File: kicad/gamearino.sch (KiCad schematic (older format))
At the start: 11 parts, among them Q3 PMBT3904, Q4 PMBT3906, SW1 Left, SW2 Up, SW3 Down, SW4 Right, SW5 Select, SW6 Start, SW7 B, SW8 A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

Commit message: PCB-Platzierung, 3D-Knöpfe, Schaltung wird noch getestet
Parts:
- removed Q3: PMBT3904, Package_TO_SOT_SMD:SOT-23, symbol Device:Q_NPN_BEC
- removed Q4: PMBT3906, Package_TO_SOT_SMD:SOT-23, symbol Device:Q_PNP_BEC
- removed SW1: Left, htl_smd:SW_Push_5.1mm_H1.5mm, symbol Switch:SW_Push
- removed SW2: Up, htl_smd:SW_Push_5.1mm_H1.5mm, symbol Switch:SW_Push
- removed SW3: Down, htl_smd:SW_Push_5.1mm_H1.5mm, symbol Switch:SW_Push
- removed SW4: Right, htl_smd:SW_Push_5.1mm_H1.5mm, symbol Switch:SW_Push
- removed SW5: Select, htl_smd:SW_Push_5.1mm_H1.5mm, symbol Switch:SW_Push
- removed SW6: Start, htl_smd:SW_Push_5.1mm_H1.5mm, symbol Switch:SW_Push
- removed SW7: B, htl_smd:SW_Push_5.1mm_H1.5mm, symbol Switch:SW_Push
- removed SW8: A, htl_smd:SW_Push_5.1mm_H1.5mm, symbol Switch:SW_Push
- added H1, H2, H3, H4: MountingHole, MountingHole:MountingHole_3.2mm_M3, symbol Mechanical:MountingHole
- added Item1: 3D Druck: Knopf A, gamearino:ABKnopf, symbol htl_virtual:Item
- added Item2: 3D Druck: Knopf B, gamearino:ABKnopf, symbol htl_virtual:Item
- added Item3: 3D Druck: Knopf Start, gamearino:StartSelect, symbol htl_virtual:Item
- added Item4: 3D Druck: Knopf Select, gamearino:StartSelect, symbol htl_virtual:Item
- added Item5: 3D Druck: Steuerkreuz, gamearino:Steuerkreuz_zeik, symbol htl_virtual:Item
- added Item6: PCB: Abmessungen?, 2 Layer, 35u Cu, d1,6mm, symbol htl_virtual:Item
- added Item7: SMD-Schablone: 120um, Edelstahl, 25mm Umlaufender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, symbol htl_virtual:Item
- added R1, R2: 10k, Resistor_SMD:R_0603_1608Metric, symbol Device:R
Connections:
- net labels added: +3.3V, +3V3, GNDD
- wire segments 0 -> 45
- no-connect marks 0 -> 1
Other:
- note added: "Arduino-IDE:\nProgrammierbar über die Standardeinstellungen\nfür NodeMCU V1.0"
- note added: "Enable Pin:\nmuss über 10k auf 3V3 liegen"
- note added: "GPIO0 - Bootmode: \nlow=bootloader, \nhigh=flashboot"
- note added: "GPIO15:\nmuss beim Booten über 10k\nauf GND liegen. Dann kann er\nverwendet werden."
- note added: "TODO: SDA/SCL an ESP ausprobieren"
- moved on the sheet: U1

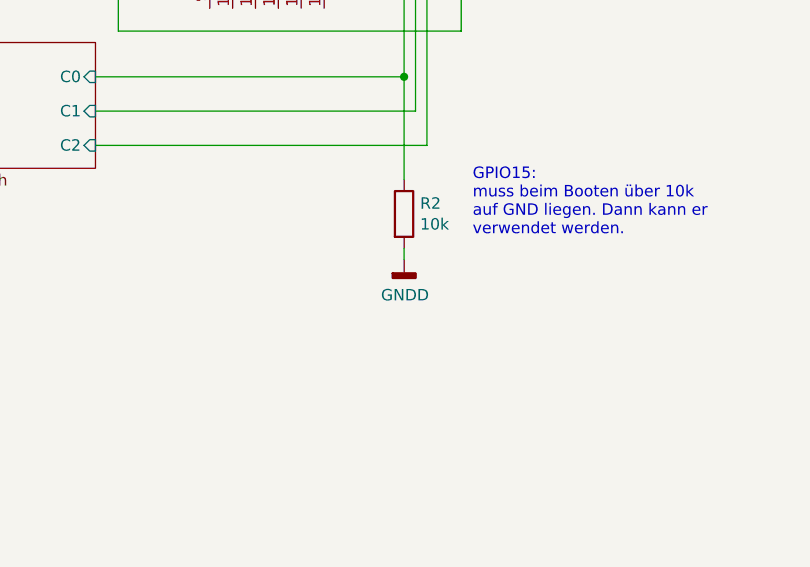
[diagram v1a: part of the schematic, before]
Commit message: Changelog eingeführt, GND statt GNDD
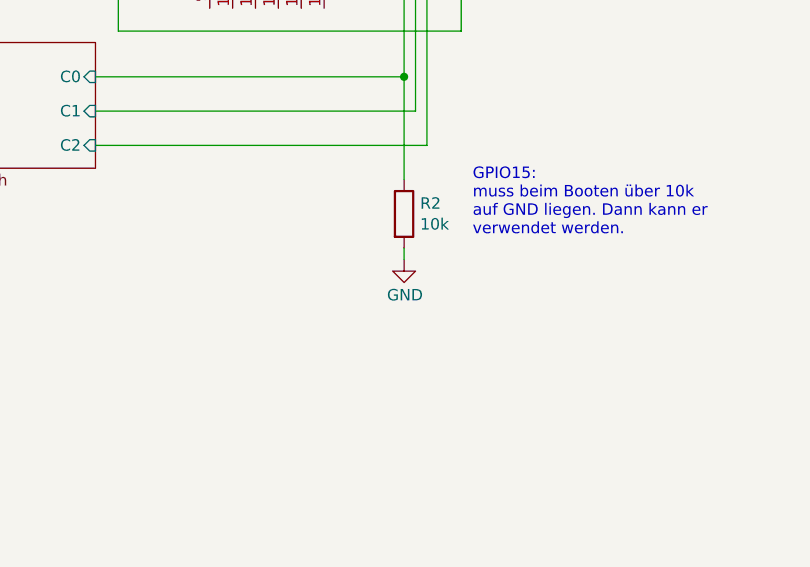
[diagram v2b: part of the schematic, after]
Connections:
- net GNDD renamed GND
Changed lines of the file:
@@
 	6350 3950 6300 3950
 $Comp
-L power:GNDD #PWR?
+L power:GND #PWR?
 U 1 1 6040EFD2
 P 6350 5550
@@
 AR Path="/6040EFD2" Ref="#PWR02"  Part="1"
 F 0 "#PWR02" H 6350 5300 50  0001 C CNN
-F 1 "GNDD" H 6354 5395 50  0000 C CNN
+F 1 "GND" H 6354 5395 50  0000 C CNN
 F 2 "" H 6350 5550 50  0001 C CNN
 F 3 "" H 6350 5550 50  0001 C CNN

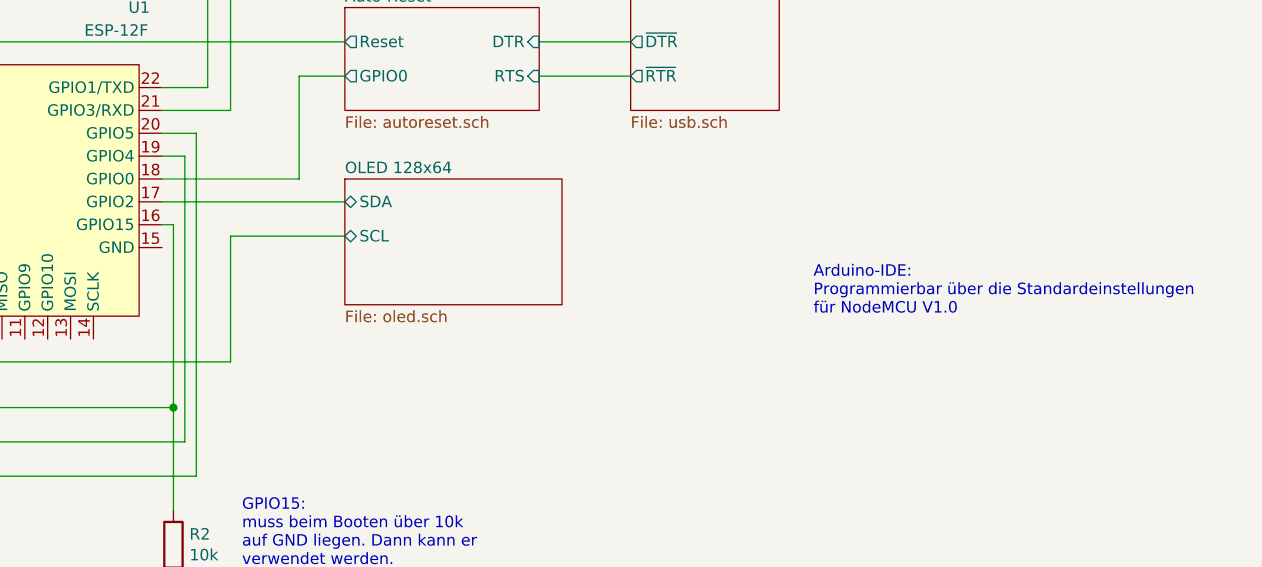
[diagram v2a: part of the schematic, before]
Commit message: usb.sch Datei war gebrochen, wurde gefixt
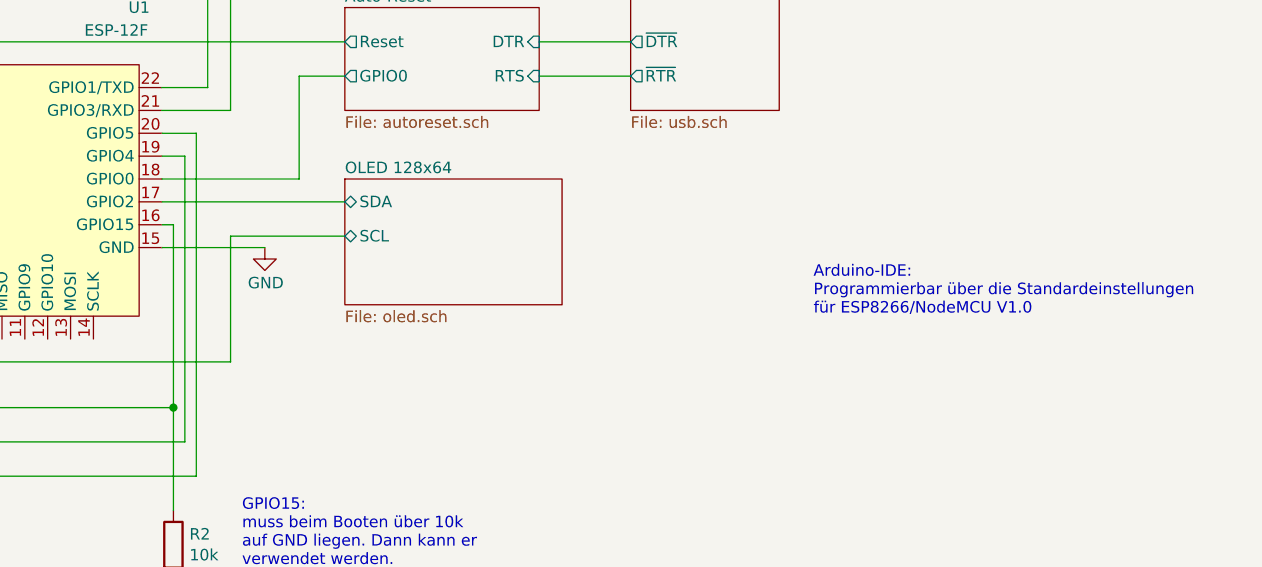
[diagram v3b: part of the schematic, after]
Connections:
- net GND: now also U1.15 (GND)
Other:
- note added: "Arduino-IDE:\nProgrammierbar über die Standardeinstellungen\nfür ESP8266/NodeMCU V1.0"
- note removed: "Arduino-IDE:\nProgrammierbar über die Standardeinstellungen\nfür NodeMCU V1.0"
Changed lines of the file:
@@
 GPIO15:\nmuss beim Booten über 10k\nauf GND liegen. Dann kann er\nverwendet werden.
 Text Notes 9150 4350 0    50   ~ 0
-Arduino-IDE:\nProgrammierbar über die Standardeinstellungen\nfür NodeMCU V1.0
+Arduino-IDE:\nProgrammierbar über die Standardeinstellungen\nfür ESP8266/NodeMCU V1.0
 $Comp
 L htl_virtual:Item Item1
@@
 	1    0    0    -1
 $EndComp
+$Comp
+L power:GND #PWR?
+U 1 1 60538B2A
+P 6750 4050
+AR Path="/5F8674B3/60538B2A" Ref="#PWR?"  Part="1"
+AR Path="/60538B2A" Ref="#PWR?"  Part="1"
+F 0 "#PWR?" H 6750 3800 50  0001 C CNN
+F 1 "GND" H 6754 3895 50  0000 C CNN
+F 2 "" H 6750 4050 50  0001 C CNN
+F 3 "" H 6750 4050 50  0001 C CNN
+	1    6750 4050
+	1    0    0    -1
+$EndComp
+Wire Wire Line
+	6300 4050 6750 4050
 $EndSCHEMATC

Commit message: Pinliste und kleinere Verschönerungen, Transistor-Value, ...
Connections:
- no-connect marks 1 -> 7
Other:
- note added: "TODO: SDA-Leitung macht \ndas Flashen aktuell unmöglich."
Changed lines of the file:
@@
 Wire Wire Line
 	6300 4050 6750 4050
+NoConn ~ 5500 4450
+NoConn ~ 5600 4450
+NoConn ~ 5700 4450
+NoConn ~ 5800 4450
+NoConn ~ 5900 4450
+NoConn ~ 6000 4450
+Text Notes 7150 4700 0    50   ~ 0
+TODO: SDA-Leitung macht \ndas Flashen aktuell unmöglich.
+Wire Notes Line
+	7100 4600 6800 3850
 $EndSCHEMATC

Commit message: OLED funktioniert, Gehäuse vorläufig fertig
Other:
- note added: "TODO: Neue 3D-Modelle verwenden"
- note added: "TODO: Taster ausprobieren"
- note removed: "TODO: SDA-Leitung macht \ndas Flashen aktuell unmöglich."
- note removed: "TODO: SDA/SCL an ESP ausprobieren"
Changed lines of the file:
@@
 Text Notes 5950 2300 0    50   ~ 0
 GPIO0 - Bootmode: \nlow=bootloader, \nhigh=flashboot
-Text Notes 1050 750  0    50   ~ 0
-TODO: SDA/SCL an ESP ausprobieren
 Wire Wire Line
 	6300 3350 6500 3350
@@
 NoConn ~ 5900 4450
 NoConn ~ 6000 4450
-Text Notes 7150 4700 0    50   ~ 0
-TODO: SDA-Leitung macht \ndas Flashen aktuell unmöglich.
-Wire Notes Line
-	7100 4600 6800 3850
+Text Notes 3750 5700 0    50   ~ 0
+TODO: Taster ausprobieren
+Text Notes 2050 6350 0    50   ~ 0
+TODO: Neue 3D-Modelle verwenden
 $EndSCHEMATC

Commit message: v0.0.1 für CNC-Fertigung
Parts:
- H1, H2, H3, H4: footprint MountingHole:MountingHole_3.2mm_M3 -> htl_mechanical:MountingHole_3.2mm_M3
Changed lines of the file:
@@
 F 0 "H1" H 10400 5796 50  0000 L CNN
 F 1 "MountingHole" H 10400 5705 50  0000 L CNN
-F 2 "MountingHole:MountingHole_3.2mm_M3" H 10300 5750 50  0001 C CNN
+F 2 "htl_mechanical:MountingHole_3.2mm_M3" H 10300 5750 50  0001 C CNN
 F 3 "~" H 10300 5750 50  0001 C CNN
 	1    10300 5750
@@
 F 0 "H2" H 10400 5996 50  0000 L CNN
 F 1 "MountingHole" H 10400 5905 50  0000 L CNN
-F 2 "MountingHole:MountingHole_3.2mm_M3" H 10300 5950 50  0001 C CNN
+F 2 "htl_mechanical:MountingHole_3.2mm_M3" H 10300 5950 50  0001 C CNN
 F 3 "~" H 10300 5950 50  0001 C CNN
 	1    10300 5950
@@
 F 0 "H3" H 10400 6196 50  0000 L CNN
 F 1 "MountingHole" H 10400 6105 50  0000 L CNN
-F 2 "MountingHole:MountingHole_3.2mm_M3" H 10300 6150 50  0001 C CNN
+F 2 "htl_mechanical:MountingHole_3.2mm_M3" H 10300 6150 50  0001 C CNN
 F 3 "~" H 10300 6150 50  0001 C CNN
 	1    10300 6150
@@
 F 0 "H4" H 10400 6396 50  0000 L CNN
 F 1 "MountingHole" H 10400 6305 50  0000 L CNN
-F 2 "MountingHole:MountingHole_3.2mm_M3" H 10300 6350 50  0001 C CNN
+F 2 "htl_mechanical:MountingHole_3.2mm_M3" H 10300 6350 50  0001 C CNN
 F 3 "~" H 10300 6350 50  0001 C CNN
 	1    10300 6350
@@
 P 6750 4050
 AR Path="/5F8674B3/60538B2A" Ref="#PWR?"  Part="1"
-AR Path="/60538B2A" Ref="#PWR?"  Part="1"
-F 0 "#PWR?" H 6750 3800 50  0001 C CNN
+AR Path="/60538B2A" Ref="#PWR0102"  Part="1"
+F 0 "#PWR0102" H 6750 3800 50  0001 C CNN
 F 1 "GND" H 6754 3895 50  0000 C CNN
 F 2 "" H 6750 4050 50  0001 C CNN

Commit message: Fertiges Layout v0.0.2, 3 Stk bestellt
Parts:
- added FID1, FID2: Fiducial, htl_mechanical:paste-fiducial, symbol Mechanical:Fiducial
- Item1, Item2: footprint gamearino:ABKnopf -> gamearino:ABKnopf_v2
- Item3, Item4: footprint gamearino:StartSelect -> gamearino:StartSelect_v2
- Item5: footprint gamearino:Steuerkreuz_zeik -> gamearino:Steuerkreuz_zeik_v2
- U1: DistOrderNr (none) -> C82891; Distributor (none) -> LCSC; ManPartNr (none) -> ESP-12F(ESP8266MOD); Manufacturer (none) -> Ai-Thinker; PriceEUR (none) -> 1.24; PriceForQty (none) -> 100; Weblink (none) -> https://lcsc.com/product-detail/WiFi-Modules_Ai-Thinker-ESP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
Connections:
- net EN: now reaches R1.2, U1.3 (EN)
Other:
- note removed: "TODO: Neue 3D-Modelle verwenden"
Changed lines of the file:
@@
 Sheet 1 5
 Title "Gamearino"
-Date "2020-10-13"
-Rev "20.0.0-dev"
+Date "2021-04-29"
+Rev "V0.0.2"
 Comp "HTL-Steyr"
 Comment1 "4ABHEL, 2020/2021"
-Comment2 ""
+Comment2 "Hosted by Prof. Karl Zeilhofer"
 Comment3 ""
 Comment4 ""
@@
 F 2 "htl_modules:ESP-12F" H 5750 3850 50  0001 C CNN
 F 3 "http://wiki.ai-thinker.com/_media/esp8266/esp8266_series_modules_user_manual_v1.1.pdf" H 5400 3950 50  0001 C CNN
+F 4 "C82891" H 5750 3850 50  0001 C CNN "DistOrderNr"
+F 5 "LCSC" H 5750 3850 50  0001 C CNN "Distributor"
+F 6 "ESP-12F(ESP8266MOD)" H 5750 3850 50  0001 C CNN "ManPartNr"
+F 7 "Ai-Thinker" H 5750 3850 50  0001 C CNN "Manufacturer"
+F 8 "1.24" H 5750 3850 50  0001 C CNN "PriceEUR"
+F 9 "100" H 5750 3850 50  0001 C CNN "PriceForQty"
+F 10 "https://lcsc.com/product-detail/WiFi-Modules_Ai-Thinker-ESP-12F-ESP8266MOD_C82891.html" H 5750 3850 50  0001 C CNN "Weblink"
 	1    5750 3850
 	1    0    0    -1
@@
 P 4900 2850
 AR Path="/5F8674B3/60406C3E" Ref="#PWR?"  Part="1"
-AR Path="/60406C3E" Ref="#PWR01"  Part="1"
+AR Path="/60406C3E" Ref="#PWR02"  Part="1"
 AR Path="/603FCB6F/60406C3E" Ref="#PWR?"  Part="1"
-F 0 "#PWR01" H 4900 2700 50  0001 C CNN
+F 0 "#PWR02" H 4900 2700 50  0001 C CNN
 F 1 "+3.3V" H 4915 3023 50  0000 C CNN
 F 2 "" H 4900 2850 50  0001 C CNN
@@
 P 6350 5550
 AR Path="/5F8674B3/6040EFD2" Ref="#PWR?"  Part="1"
-AR Path="/6040EFD2" Ref="#PWR02"  Part="1"
-F 0 "#PWR02" H 6350 5300 50  0001 C CNN
+AR Path="/6040EFD2" Ref="#PWR03"  Part="1"
+F 0 "#PWR03" H 6350 5300 50  0001 C CNN
 F 1 "GND" H 6354 5395 50  0000 C CNN
 F 2 "" H 6350 5550 50  0001 C CNN
@@
 AR Path="/5FA85ABF/5F7FB5B8/60461F5A" Ref="#PWR?"  Part="1"
 AR Path="/5F8D661A/60461F5A" Ref="#PWR?"  Part="1"
-AR Path="/60461F5A" Ref="#PWR0101"  Part="1"
-F 0 "#PWR0101" H 4800 4100 50  0001 C CNN
+AR Path="/60461F5A" Ref="#PWR01"  Part="1"
+F 0 "#PWR01" H 4800 4100 50  0001 C CNN
 F 1 "+3V3" H 4815 4423 50  0000 C CNN
 F 2 "" H 4800 4250 50  0001 C CNN
@@
 F 0 "Item1" H 930 6346 50  0000 L CNN
 F 1 "3D Druck: Knopf A" H 930 6255 50  0000 L CNN
-F 2 "gamearino:ABKnopf" H 800 6230 50  0001 C CNN
+F 2 "gamearino:ABKnopf_v2" H 800 6230 50  0001 C CNN
 F 3 "~" V 800 6300 50  0001 C CNN
 	1    800  6300
@@
 F 0 "Item2" H 930 6546 50  0000 L CNN
 F 1 "3D Druck: Knopf B" H 930 6455 50  0000 L CNN
-F 2 "gamearino:ABKnopf" H 800 6430 50  0001 C CNN
+F 2 "gamearino:ABKnopf_v2" H 800 6430 50  0001 C CNN
 F 3 "~" V 800 6500 50  0001 C CNN
 	1    800  6500
@@
 F 0 "Item3" H 930 6746 50  0000 L CNN
 F 1 "3D Druck: Knopf Start" H 930 6655 50  0000 L CNN
-F 2 "gamearino:StartSelect" H 800 6630 50  0001 C CNN
+F 2 "gamearino:StartSelect_v2" H 800 6630 50  0001 C CNN
 F 3 "~" V 800 6700 50  0001 C CNN
 	1    800  6700
@@
 F 0 "Item4" H 930 6946 50  0000 L CNN
 F 1 "3D Druck: Knopf Select" H 930 6855 50  0000 L CNN
-F 2 "gamearino:StartSelect" H 800 6830 50  0001 C CNN
+F 2 "gamearino:StartSelect_v2" H 800 6830 50  0001 C CNN
 F 3 "~" V 800 6900 50  0001 C CNN
 	1    800  6900
@@
 F 0 "Item5" H 930 7146 50  0000 L CNN
 F 1 "3D Druck: Steuerkreuz" H 930 7055 50  0000 L CNN
-F 2 "gamearino:Steuerkreuz_zeik" H 800 7030 50  0001 C CNN
+F 2 "gamearino:Steuerkreuz_zeik_v2" H 800 7030 50  0001 C CNN
 F 3 "~" V 800 7100 50  0001 C CNN
 	1    800  7100
@@
 P 6750 4050
 AR Path="/5F8674B3/60538B2A" Ref="#PWR?"  Part="1"
-AR Path="/60538B2A" Ref="#PWR0102"  Part="1"
-F 0 "#PWR0102" H 6750 3800 50  0001 C CNN
+AR Path="/60538B2A" Ref="#PWR04"  Part="1"
+F 0 "#PWR04" H 6750 3800 50  0001 C CNN
 F 1 "GND" H 6754 3895 50  0000 C CNN
 F 2 "" H 6750 4050 50  0001 C CNN
@@
 Text Notes 3750 5700 0    50   ~ 0
 TODO: Taster ausprobieren
-Text Notes 2050 6350 0    50   ~ 0
-TODO: Neue 3D-Modelle verwenden
+Text Label 5000 3550 0    30   ~ 0
+EN
+$Comp
+L Mechanical:Fiducial FID1
+U 1 1 6090F4D5
+P 9500 5800
+F 0 "FID1" H 9585 5846 50  0000 L CNN
+F 1 "Fiducial" H 9585 5755 50  0000 L CNN
+F 2 "htl_mechanical:paste-fiducial" H 9500 5800 50  0001 C CNN
+F 3 "~" H 9500 5800 50  0001 C CNN
+	1    9500 5800
+	1    0    0    -1
+$EndComp
+$Comp
+L Mechanical:Fiducial FID2
+U 1 1 6090F84F
+P 9500 6000
+F 0 "FID2" H 9585 6046 50  0000 L CNN
+F 1 "Fiducial" H 9585 5955 50  0000 L CNN
+F 2 "htl_mechanical:paste-fiducial" H 9500 6000 50  0001 C CNN
+F 3 "~" H 9500 6000 50  0001 C CNN
+	1    9500 6000
+	1    0    0    -1
+$EndComp
 $EndSCHEMATC

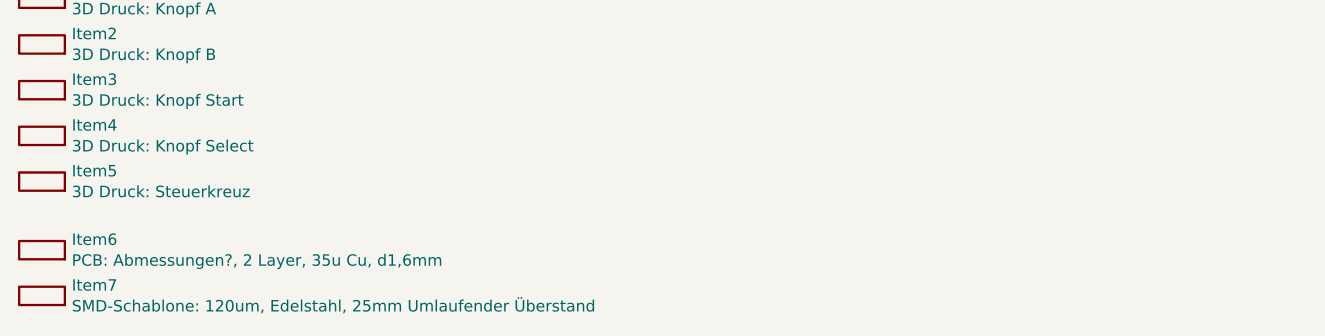
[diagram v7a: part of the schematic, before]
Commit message: BOM fertig eingepflegt
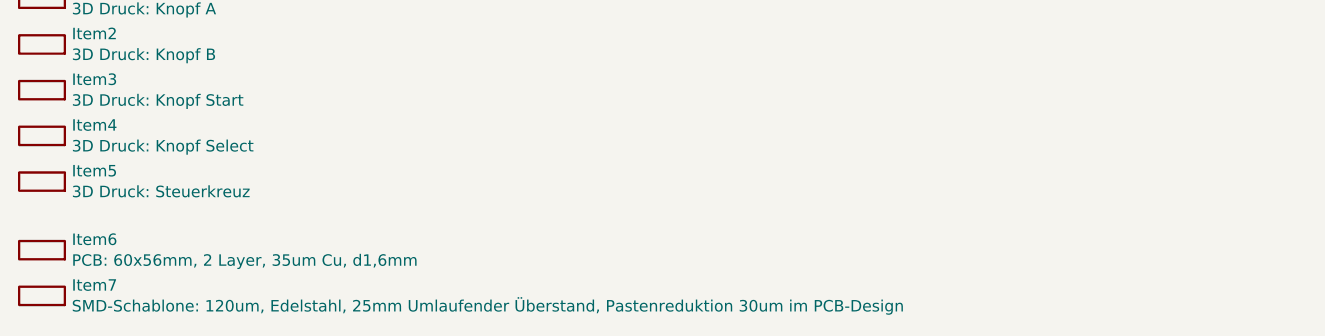
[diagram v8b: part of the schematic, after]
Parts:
- Item6: value PCB: Abmessungen?, 2 Layer, 35u Cu, d1,6mm -> PCB: 60x56mm, 2 Layer, 35um Cu, d1,6mm
- Item7: value SMD-Schablone: 120um, Edelstahl, 25mm Umlaufender Überstand -> SMD-Schablone: 120um, Edelstahl, 25mm Umlaufender Überstand, Pastenreduktion 30um im PCB-Design
- R1, R2: DistOrderNr (none) -> C103210; Distributor (none) -> LCSC; ManPartNr (none) -> RTT03103JTP; Manufacturer (none) -> RALEC; Notes (none) -> 10kΩ ±5% 0.1W ±100ppm/℃; PriceEUR (none) -> 0.0015; PriceForQty (none) -> 100
- U1: Notes (none) -> Mikrocontroller, 32 Bit, WLAN, 3.3V, 4MB Flash; PriceEUR 1.24 -> 1.243; PriceForQty 100 -> 10
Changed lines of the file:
@@
 F 6 "ESP-12F(ESP8266MOD)" H 5750 3850 50  0001 C CNN "ManPartNr"
 F 7 "Ai-Thinker" H 5750 3850 50  0001 C CNN "Manufacturer"
-F 8 "1.24" H 5750 3850 50  0001 C CNN "PriceEUR"
-F 9 "100" H 5750 3850 50  0001 C CNN "PriceForQty"
+F 8 "1.243" H 5750 3850 50  0001 C CNN "PriceEUR"
+F 9 "10" H 5750 3850 50  0001 C CNN "PriceForQty"
 F 10 "https://lcsc.com/product-detail/WiFi-Modules_Ai-Thinker-ESP-12F-ESP8266MOD_C82891.html" H 5750 3850 50  0001 C CNN "Weblink"
+F 11 "Mikrocontroller, 32 Bit, WLAN, 3.3V, 4MB Flash" H 5750 3850 50  0001 C CNN "Notes"
 	1    5750 3850
 	1    0    0    -1
@@
 F 2 "Resistor_SMD:R_0603_1608Metric" V 4830 3100 50  0001 C CNN
 F 3 "~" H 4900 3100 50  0001 C CNN
+F 4 "C103210" H 4900 3100 50  0001 C CNN "DistOrderNr"
+F 5 "LCSC" H 4900 3100 50  0001 C CNN "Distributor"
+F 6 "RTT03103JTP" H 4900 3100 50  0001 C CNN "ManPartNr"
+F 7 "RALEC" H 4900 3100 50  0001 C CNN "Manufacturer"
+F 8 "10kΩ ±5% 0.1W ±100ppm/℃" H 4900 3100 50  0001 C CNN "Notes"
+F 9 "0.0015" H 4900 3100 50  0001 C CNN "PriceEUR"
+F 10 "100" H 4900 3100 50  0001 C CNN "PriceForQty"
 	1    4900 3100
 	1    0    0    -1
@@
 F 2 "Resistor_SMD:R_0603_1608Metric" V 6280 5350 50  0001 C CNN
 F 3 "~" H 6350 5350 50  0001 C CNN
+F 4 "C103210" H 6350 5350 50  0001 C CNN "DistOrderNr"
+F 5 "LCSC" H 6350 5350 50  0001 C CNN "Distributor"
+F 6 "RTT03103JTP" H 6350 5350 50  0001 C CNN "ManPartNr"
+F 7 "RALEC" H 6350 5350 50  0001 C CNN "Manufacturer"
+F 8 "10kΩ ±5% 0.1W ±100ppm/℃" H 6350 5350 50  0001 C CNN "Notes"
+F 9 "0.0015" H 6350 5350 50  0001 C CNN "PriceEUR"
+F 10 "100" H 6350 5350 50  0001 C CNN "PriceForQty"
 	1    6350 5350
 	1    0    0    -1
@@
 P 800 7400
 F 0 "Item6" H 930 7446 50  0000 L CNN
-F 1 "PCB: Abmessungen?, 2 Layer, 35u Cu, d1,6mm" H 930 7355 50  0000 L CNN
+F 1 "PCB: 60x56mm, 2 Layer, 35um Cu, d1,6mm" H 930 7355 50  0000 L CNN
 F 2 "" H 800 7330 50  0001 C CNN
 F 3 "~" V 800 7400 50  0001 C CNN
@@
 P 800 7600
 F 0 "Item7" H 930 7646 50  0000 L CNN
-F 1 "SMD-Schablone: 120um, Edelstahl, 25mm Umlaufender Überstand" H 930 7555 50  0000 L CNN
+F 1 "SMD-Schablone: 120um, Edelstahl, 25mm Umlaufender Überstand, Pastenreduktion 30um im PCB-Design" H 930 7555 50  0000 L CNN
 F 2 "" H 800 7530 50  0001 C CNN
 F 3 "~" V 800 7600 50  0001 C CNN
